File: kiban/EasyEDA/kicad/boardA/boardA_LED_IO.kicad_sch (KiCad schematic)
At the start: 23 parts, among them U6 TPS566238P

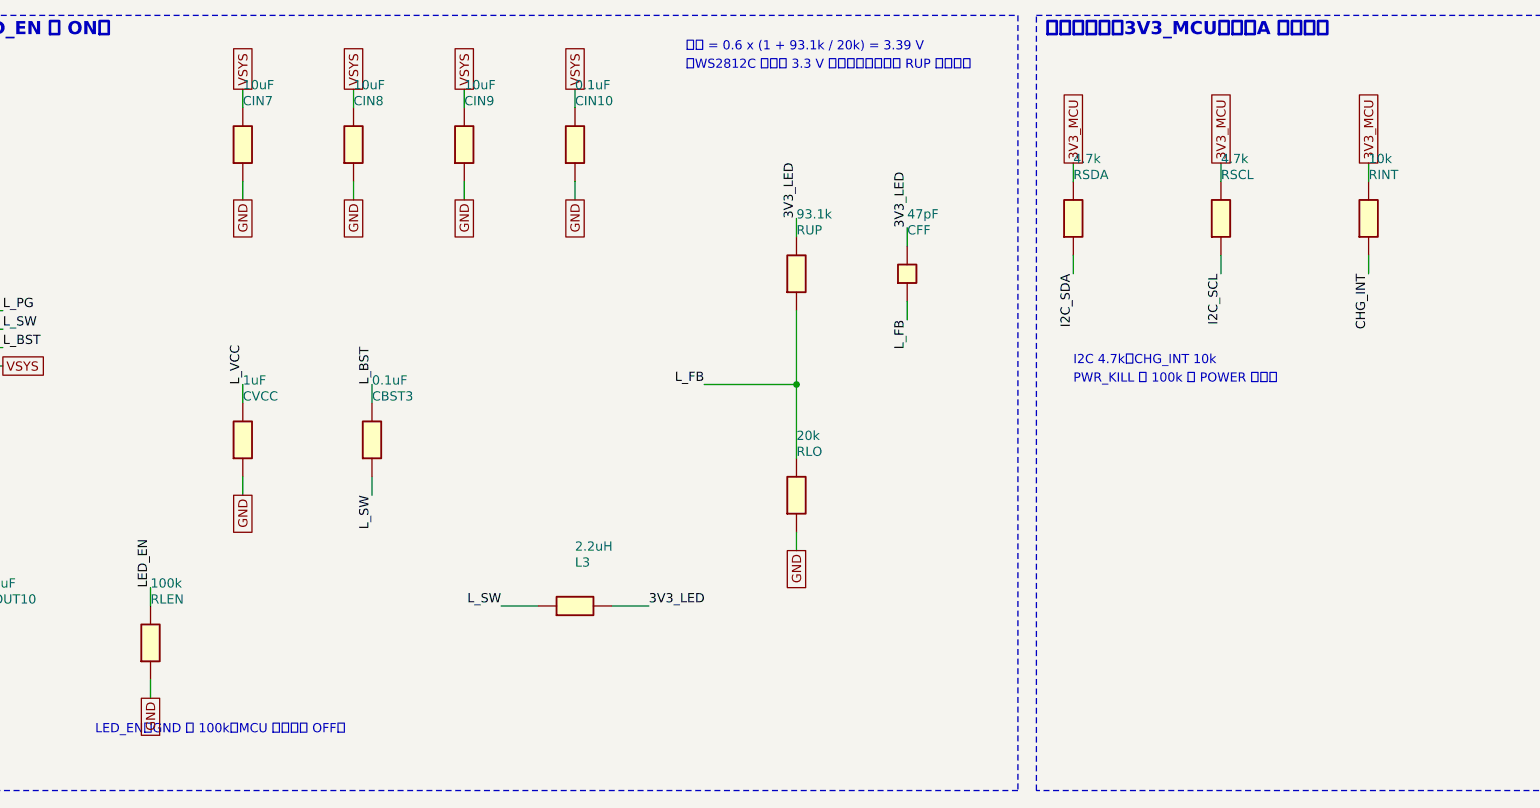
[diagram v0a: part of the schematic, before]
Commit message: feat: KiCad 版の回路図に LCSC のシンボル・フットプリントを使う (easyeda2kicad)
- tools/kicad/lcsc_lib.py: LCSC 部品を easyeda2kicad で取得し、3D パスを直して KiCad 10 形式に更新、
  boardA / boardB に lcsc ライブラリを登録 (未取得の部品だけを、間隔を空けて取得)
- kicad_export.py: 取得したシンボルを、EasyEDA とピン位置が一致する向きで使い、フットプリントを割り当てる
  (合わない部品と未取得の部品は従来の矩形シンボル)。回転した部品の値の文字は横書きのまま
- 47 種類中 30 種類を取得 (残りは EasyEDA API の 403 で未取得)。111 部品中 82 部品が LCSC のシンボル
- kicad-cli のネットリストは基板A 23 / 基板B 43 ネットとも EasyEDA と一致
- 3D モデル (lcsc.3dshapes) と KiCad の .history/ は Git に入れない

Co-Authored-By: Claude Opus 5.5 <noreply@anthropic.com>
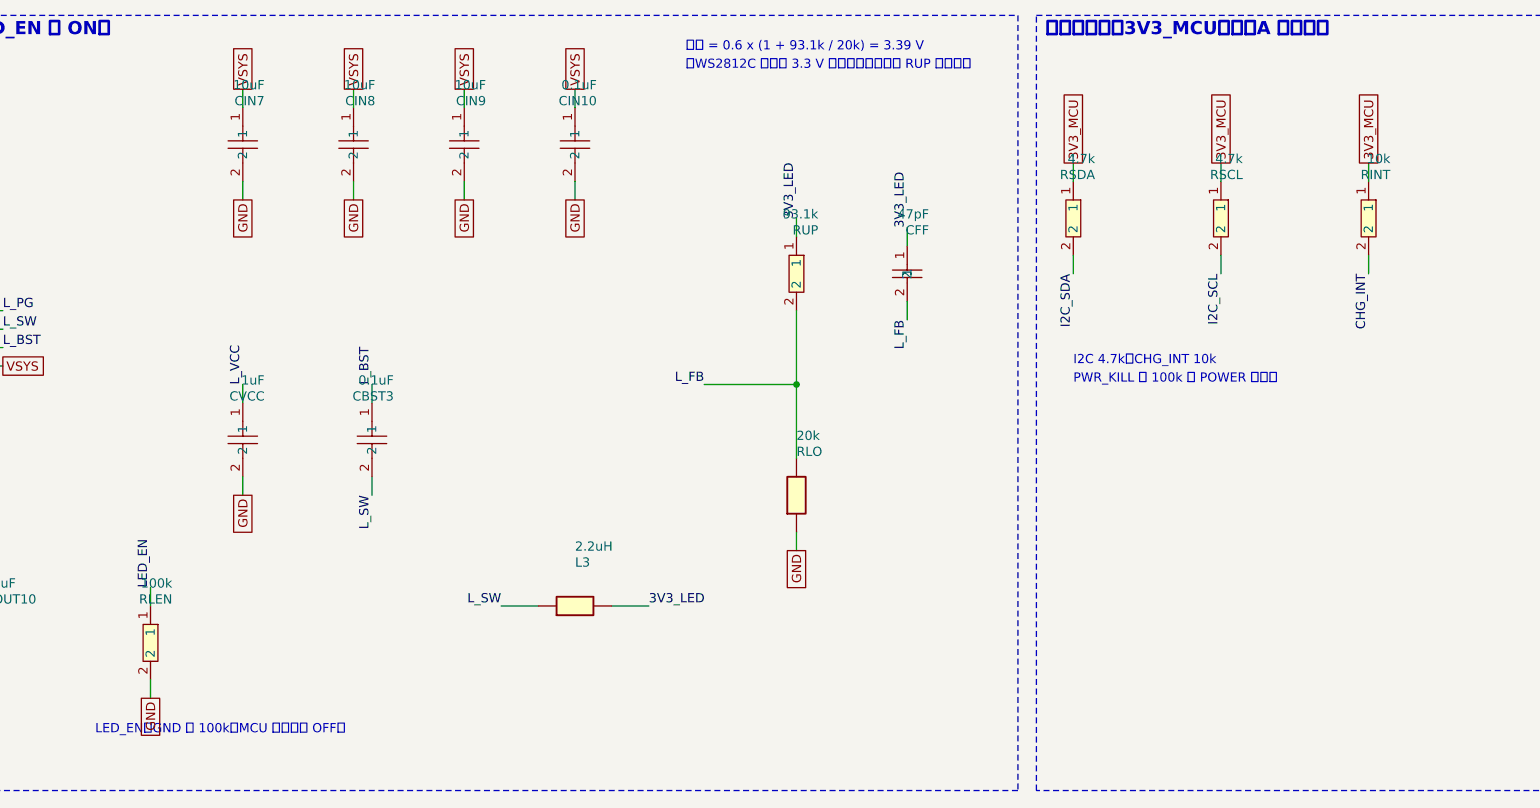
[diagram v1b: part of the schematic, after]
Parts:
- CBST3: footprint (none) -> lcsc:C0603; symbol gen:CBST_C1591_r270 -> lcsc:CL10B104KB8NNNC
- CFF: footprint (none) -> lcsc:C0603; symbol gen:CFF_C1671_r270 -> lcsc:CL10C470JB8NNNC
- CIN10: footprint (none) -> lcsc:C0603; symbol gen:CIN_C1591_r270 -> lcsc:CL10B104KB8NNNC
- CIN7, CIN8, CIN9: footprint (none) -> lcsc:C0805; symbol gen:CIN_C15850_r270 -> lcsc:CL21A106KAYNNNE
- CVCC: footprint (none) -> lcsc:C0603; symbol gen:CVCC_C15849_r270 -> lcsc:CL10A105KB8NNNC
- RINT: footprint (none) -> lcsc:R0603; symbol gen:RINT_C25804_r270 -> lcsc:0603WAF1002T5E
- RLEN: footprint (none) -> lcsc:R0603; symbol gen:RLEN_C25803_r270 -> lcsc:0603WAF1003T5E
- RSCL: footprint (none) -> lcsc:R0603; symbol gen:RSCL_C23162_r270 -> lcsc:0603WAF4701T5E
- RSDA: footprint (none) -> lcsc:R0603; symbol gen:RSDA_C23162_r270 -> lcsc:0603WAF4701T5E
- RUP: footprint (none) -> lcsc:R0603; symbol gen:RUP_C23266_r270 -> lcsc:0603WAF9312T5E
